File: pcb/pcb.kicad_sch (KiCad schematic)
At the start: 0 parts

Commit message: i forget the files before
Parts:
- added C1, C3, C5: 100nF, symbol Device:C
- added C2, C4, C6: 10uF, symbol Device:C_Polarized
- added J1: Screw_Terminal_01x02, symbol Connector:Screw_Terminal_01x02
- added J2: Conn_01x04_Pin, Connector_PinSocket_2.54mm:PinSocket_1x04_P2.54mm_Vertical, symbol Connector:Conn_01x04_Pin
- added U1: ESP32-C6-MINI-1, RF_Module:ESP32-C6-MINI-1, symbol RF_Module:ESP32-C6-MINI-1
- added U2: AMS1117-3.3, Package_TO_SOT_SMD:SOT-223-3_TabPin2, symbol Regulator_Linear:AMS1117-3.3
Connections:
- new net: J2.2 (Pin_2), U1.30 (RXD0)
- new net: J2.3 (Pin_3), U1.31 (TXD0)
- new net: C1.1, C2.1, J1.2 (Pin_2), U2.3 (VI)
- new net +3.3V: C3.1, C4.1, C5.1, C6.1, J2.4 (Pin_4), U1.3 (3V3), U2.2 (VO)
- new net GND: C1.2, C2.2, C3.2, C4.2, C5.2, C6.2, J1.1 (Pin_1), J2.1 (Pin_1), U1.1 (GND), U1.11 (GND), U1.14 (GND), U1.2 (GND), U1.36 (GND), U1.37 (GND), U1.38 (GND), U1.39 (GND), U1.40 (GND), U1.41 (GND), U1.42 (GND), U1.43 (GND), U1.44 (GND), U1.45 (GND), U1.46 (GND), U1.47 (GND), U1.48 (GND), U1.49 (GND), U1.50 (GND), U1.51 (GND), U1.52 (GND), U1.53 (GND), U2.1 (GND)

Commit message: fixing some issue
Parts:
- added J3, J4: Screw_Terminal_01x03, symbol Connector:Screw_Terminal_01x03
- renumbered U2 to U1, U1 to U2
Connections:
- net +3.3V: now also J3.3 (Pin_3), J4.3 (Pin_3)
- net GND: now also J3.1 (Pin_1), J4.1 (Pin_1)
- net at U2.10 (IO5): now also J4.2 (Pin_2)
- net at U2.6 (IO3): now also J3.2 (Pin_2)

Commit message: adding screw terminals for the sensors
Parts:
- added J5: Screw_Terminal_01x02, symbol Connector:Screw_Terminal_01x02
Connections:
- net +3.3V: now also J5.2 (Pin_2)
- net at U2.23 (IO9): now also J5.1 (Pin_1)
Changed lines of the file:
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@@
+	(wire
+		(pts
+			(xy 104.14 115.57) (xy 137.16 115.57)
+		)
+		(stroke
+			(width 0)
+			(type default)
+		)
+	)
 	(wire
 		(pts
@@
 	(wire
 		(pts
-			(xy 160.02 43.18) (xy 160.02 50.8)
+			(xy 137.16 115.57) (xy 137.16 109.22)
 		)
 		(stroke
@@
 		)
 	)
+	(wire
+		(pts
+			(xy 160.02 43.18) (xy 160.02 50.8)
+		)
+		(stroke
+			(width 0)
+			(type default)
+		)
+	)
 	(symbol
 		(lib_id "power:GND")
@@
 	)
 	(symbol
+		(lib_id "power:+3.3V")
+		(at 104.14 113.03 270)
+		(unit 1)
+		(exclude_from_sim no)
+		(in_bom yes)
+		(on_board yes)
+		(dnp no)
+		(fields_autoplaced yes)
+		(property "Reference" "#PWR012"
+			(at 100.33 113.03 0)
+			(effects
+				(font
+					(size 1.27 1.27)
+				)
+				(hide yes)
+			)
+		)
+		(property "Value" "+3.3V"
+			(at 107.95 113.0299 90)
+			(effects
+				(font
+					(size 1.27 1.27)
+				)
+				(justify left)
+			)
+		)
+		(property "Footprint" ""
+			(at 104.14 113.03 0)
+			(effects
+				(font
+					(size 1.27 1.27)
+				)
+				(hide yes)
+			)
+		)
+		(property "Datasheet" ""
+			(at 104.14 113.03 0)
+			(effects
+				(font
+					(size 1.27 1.27)
+				)
+				(hide yes)
+			)
+		)
+		(property "Description" "Power symbol creates a global label with name \"+3.3V\""
+			(at 104.14 113.03 0)
+			(effects
+				(font
+					(size 1.27 1.27)
+				)
+				(hide yes)
+			)
+		)
+		(pin "1"
+		)
+		(instances
+			(project "pcb"
+				(path "/2955ee96-3683-4cf6-bfa3-83b5e4980920"
+					(reference "#PWR012")
+					(unit 1)
+				)
+			)
+		)
+	)
+	(symbol
 		(lib_id "power:GND")
 		(at 160.02 43.18 90)
@@
 					(unit 1)
 				)
+			)
+		)
+	)
+	(symbol
+		(lib_id "Connector:Screw_Terminal_01x02")
+		(at 99.06 115.57 180)
+		(unit 1)
+		(exclude_from_sim no)
+		(in_bom yes)
+		(on_board yes)
+		(dnp no)
+		(fields_autoplaced yes)
+		(property "Reference" "J5"
+			(at 99.06 106.68 0)
+			(effects
+				(font
+					(size 1.27 1.27)
+				)
+			)
+		)
+		(property "Value" "Screw_Terminal_01x02"
+			(at 99.06 109.22 0)
+			(effects
+				(font
+					(size 1.27 1.27)
+				)
+			)
+		)
+		(property "Footprint" ""
+			(at 99.06 115.57 0)
+			(effects
+				(font
+					(size 1.27 1.27)
+				)
+				(hide yes)
+			)
+		)
+		(property "Datasheet" "~"
+			(at 99.06 115.57 0)
+			(effects
+				(font
+					(size 1.27 1.27)
+				)
+				(hide yes)
+			)
+		)
+		(property "Description" "Generic screw terminal, single row, 01x02, script generated (kicad-library-utils/schlib/autogen/connector/)"
+			(at 99.06 115.57 0)
+			(effects
+				(font
+					(size 1.27 1.27)
+				)
+				(hide yes)
+			)
+		)
+		(pin "2"
+		)
+		(pin "1"
+		)
+		(instances
+			(project "pcb"
+				(path "/2955ee96-3683-4cf6-bfa3-83b5e4980920"
+					(reference "J5")
+					(unit 1)
+				)

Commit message: the files... again
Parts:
- added J6, J7: Screw_Terminal_01x02, symbol Connector:Screw_Terminal_01x02
- added K1, K2: SANYOU_SRD_Form_A, Relay_THT:Relay_SPST_SANYOU_SRD_Series_Form_A, symbol Relay:SANYOU_SRD_Form_A
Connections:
- net GND: now also K1.2, K2.2
- net at U2.17 (IO12): now also K1.5
- net at U2.29 (IO23): now also K2.5
- new net: J7.1 (Pin_1), K2.3
- new net: J7.2 (Pin_2), K2.1
- new net: J6.2 (Pin_2), K1.1
- new net: J6.1 (Pin_1), K1.3

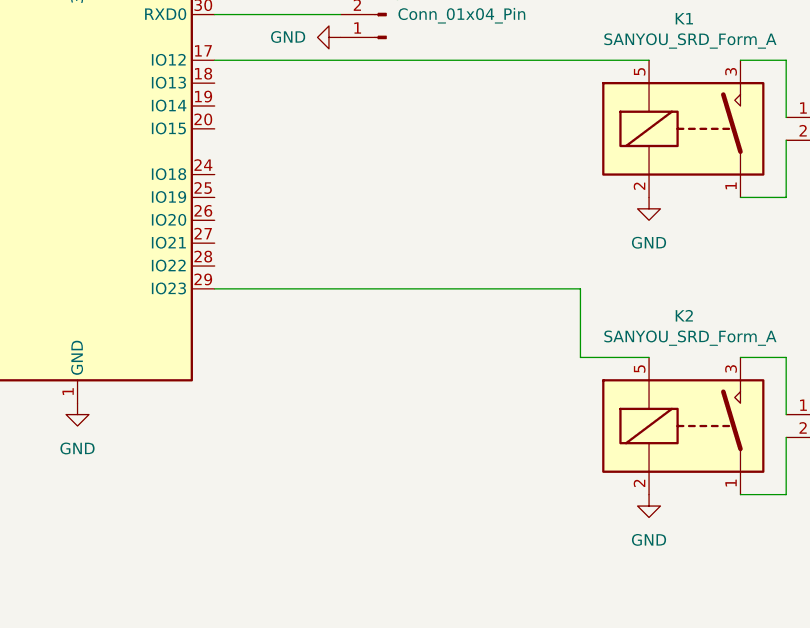
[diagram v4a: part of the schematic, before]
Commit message: adding the SPI screen
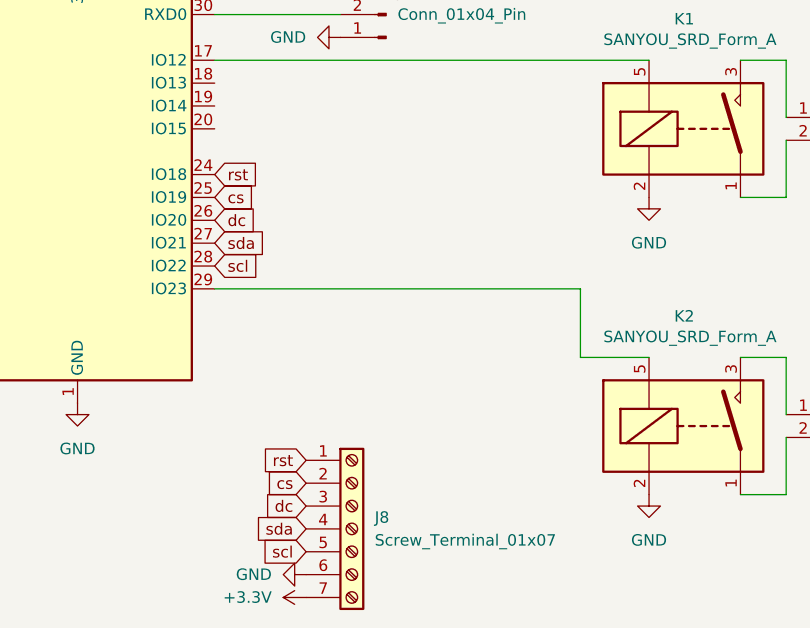
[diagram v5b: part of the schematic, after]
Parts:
- added J8: Screw_Terminal_01x07, symbol Connector:Screw_Terminal_01x07
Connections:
- net +3.3V: now also J8.7 (Pin_7)
- net GND: now also J8.6 (Pin_6)
- net rst: now reaches U2.24 (IO18)
- net rst: now also J8.1 (Pin_1)
- net cs: now reaches U2.25 (IO19)
- net cs: now also J8.2 (Pin_2)
- net dc: now reaches U2.26 (IO20)
- net dc: now also J8.3 (Pin_3)
- net sda: now reaches U2.27 (IO21)
- net sda: now also J8.4 (Pin_4)
- net scl: now reaches U2.28 (IO22)
- net scl: now also J8.5 (Pin_5)

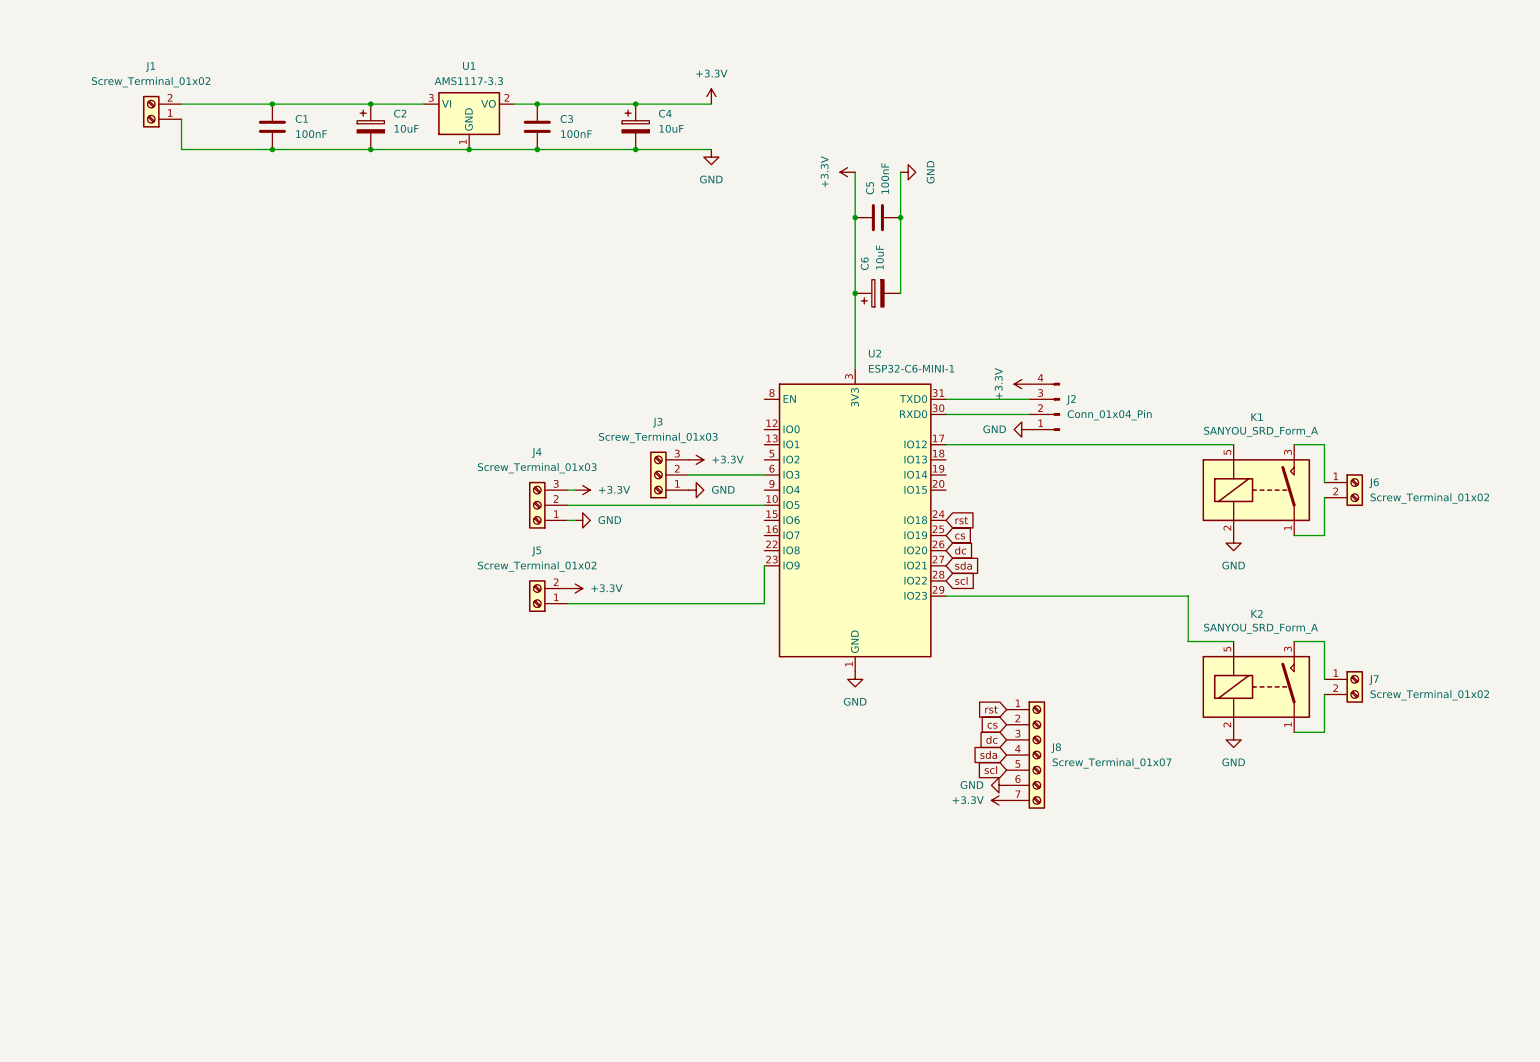
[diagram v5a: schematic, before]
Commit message: cleaning the schematic
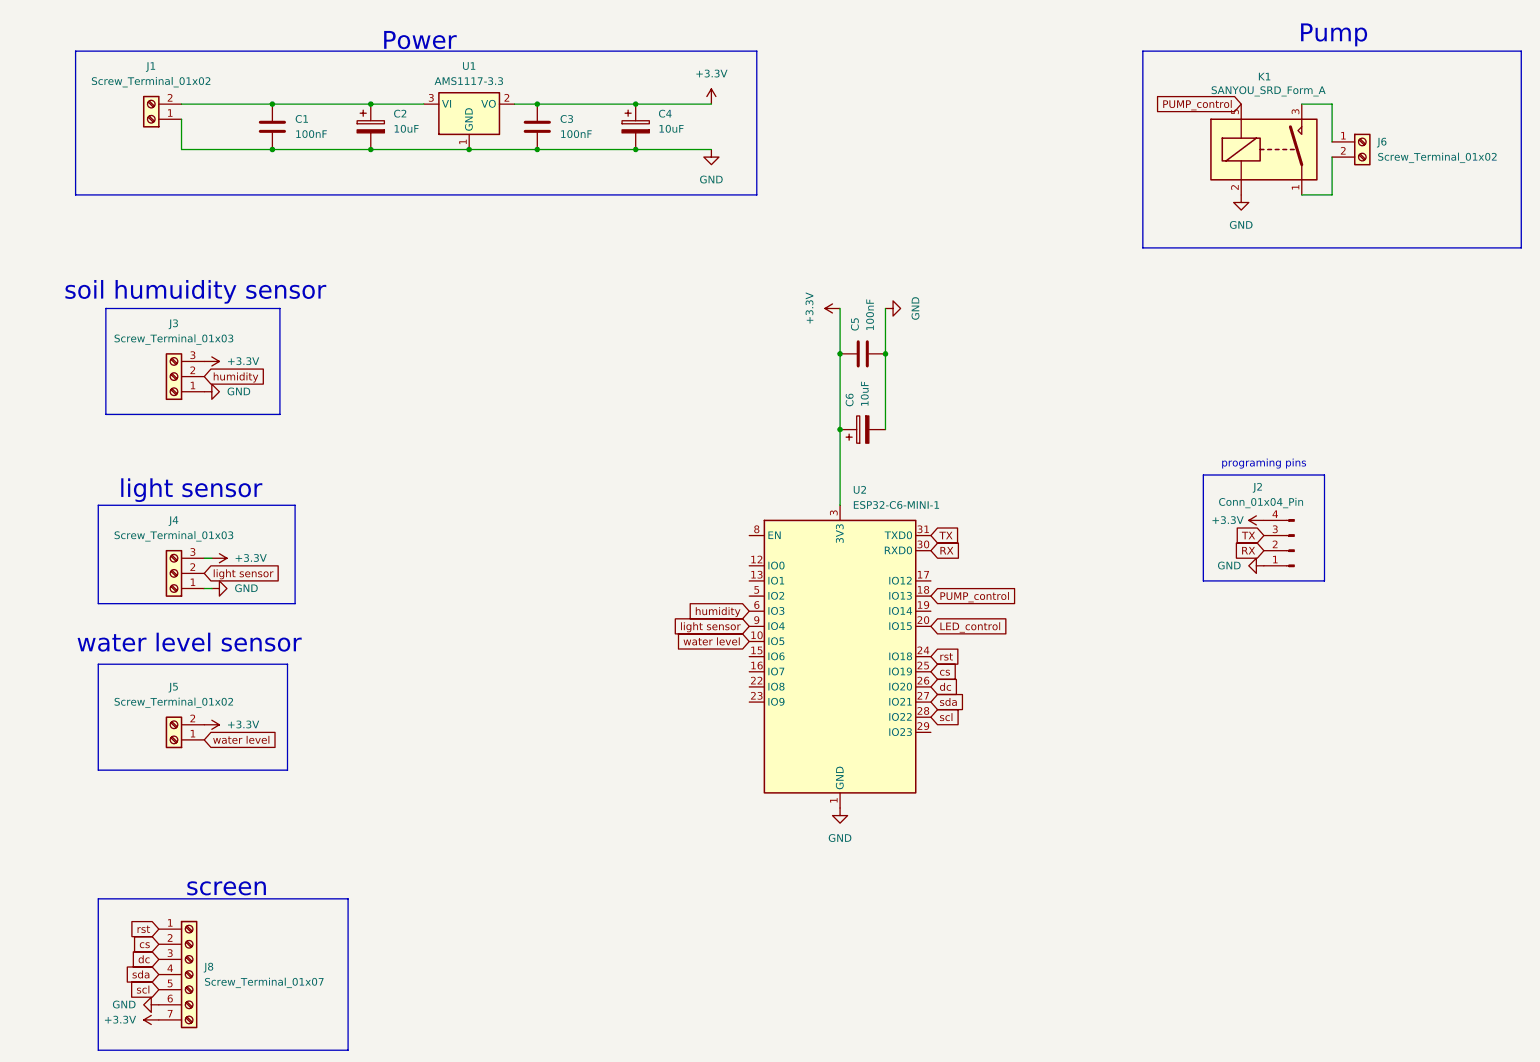
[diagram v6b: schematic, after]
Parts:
- removed J7: Screw_Terminal_01x02, symbol Connector:Screw_Terminal_01x02
- removed K2: SANYOU_SRD_Form_A, Relay_THT:Relay_SPST_SANYOU_SRD_Series_Form_A, symbol Relay:SANYOU_SRD_Form_A
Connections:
- net humidity: now reaches J3.2 (Pin_2), U2.6 (IO3)
- net RX: now reaches J2.2 (Pin_2), U2.30 (RXD0)
- net TX: now reaches J2.3 (Pin_3), U2.31 (TXD0)
- net light sensor: now reaches J4.2 (Pin_2)
- net light sensor: now also U2.9 (IO4); no longer U2.10 (IO5)
- net at U2.17 (IO12): no longer K1.5
- net PUMP_control: now reaches U2.18 (IO13)
- net PUMP_control: now also K1.5
- net LED_control: now reaches U2.20 (IO15)
- net at U2.23 (IO9): no longer J5.1 (Pin_1)
- new net water level: J5.1 (Pin_1), U2.10 (IO5)
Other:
- note added: "Power"
- note added: "Pump"
- note added: "light sensor"
- note added: "programing pins"
- note added: "screen"
- note added: "soil humuidity sensor"
- note added: "water level sensor"
- moved on the sheet: C5, C6, J2, J3, J4, J5, J6, J8, K1, U2

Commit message: Adding the MOSFET circuit
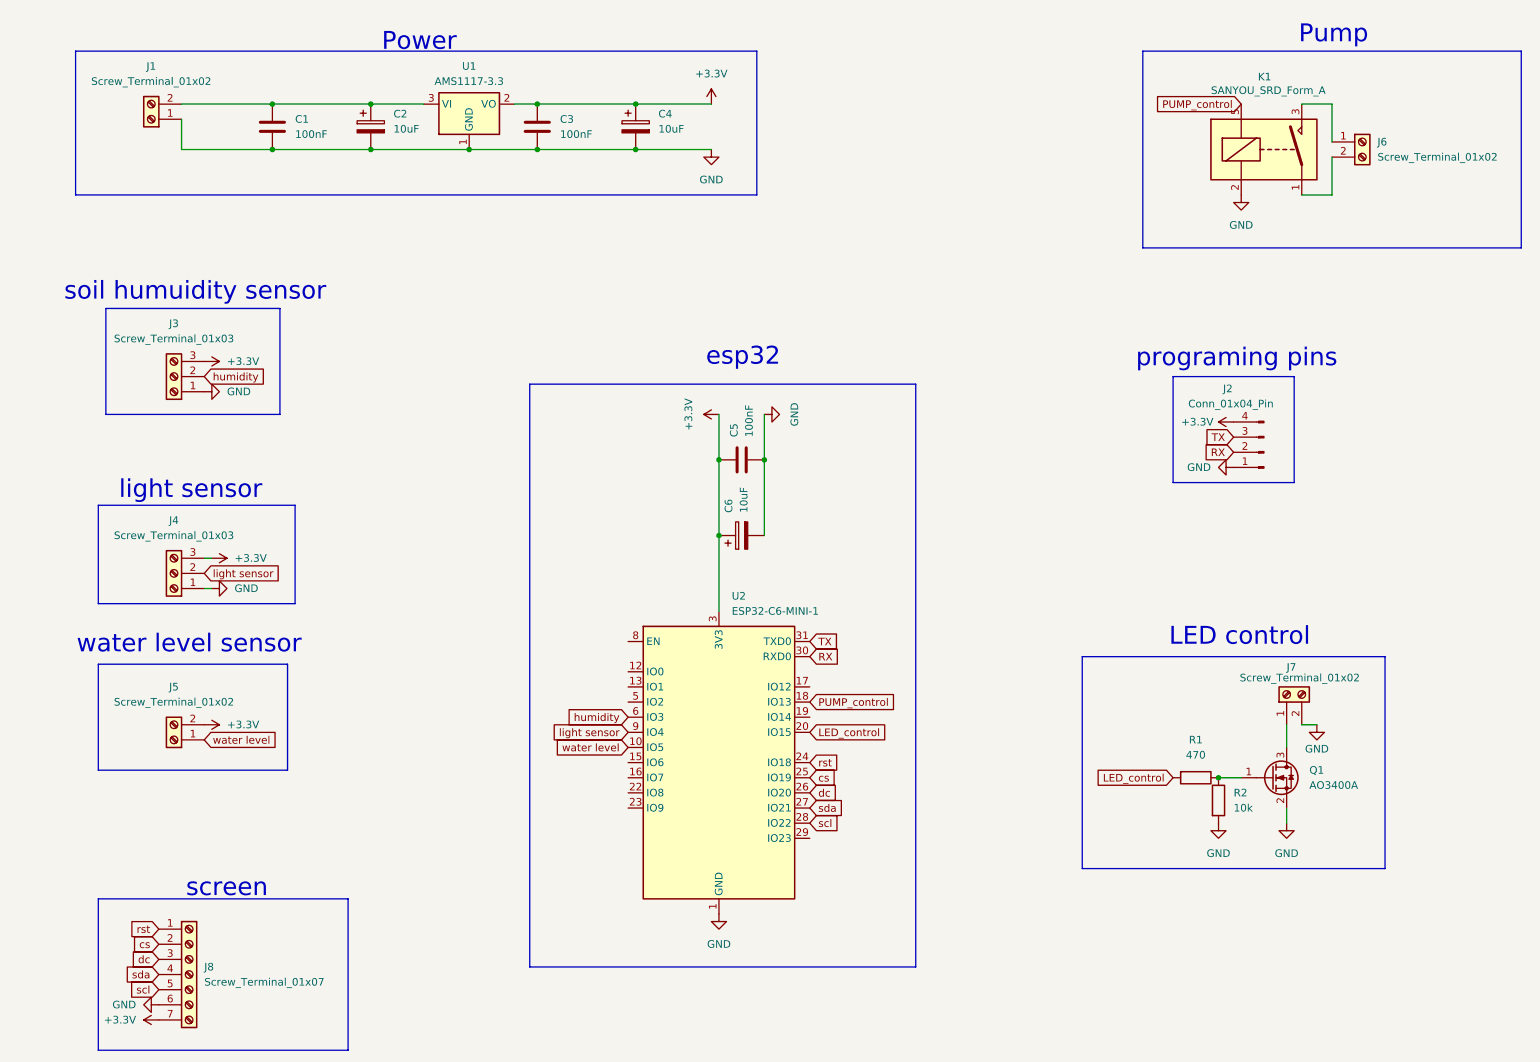
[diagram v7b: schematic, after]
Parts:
- added J7: Screw_Terminal_01x02, symbol Connector:Screw_Terminal_01x02
- added Q1: AO3400A, Package_TO_SOT_SMD:SOT-23, symbol Transistor_FET:AO3400A
- added R1: 470, symbol Device:R
- added R2: 10k, symbol Device:R
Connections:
- net GND: now also J7.2 (Pin_2), Q1.2 (S), R2.2
- net LED_control: now also R1.2
- new net: Q1.1 (G), R1.1, R2.1
- new net: J7.1 (Pin_1), Q1.3 (D)
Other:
- note added: "LED control"
- note added: "esp32"
- moved on the sheet: C5, C6, J2, U2
